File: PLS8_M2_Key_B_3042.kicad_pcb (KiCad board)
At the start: 10 copper layers, 42 x 30 mm, 39 parts, among them Q2 DTC123JUA, Q3 DTC123JUA, Q4 DTC123JUA, U20 PLS8-E, U28 M2_KEYB_3042

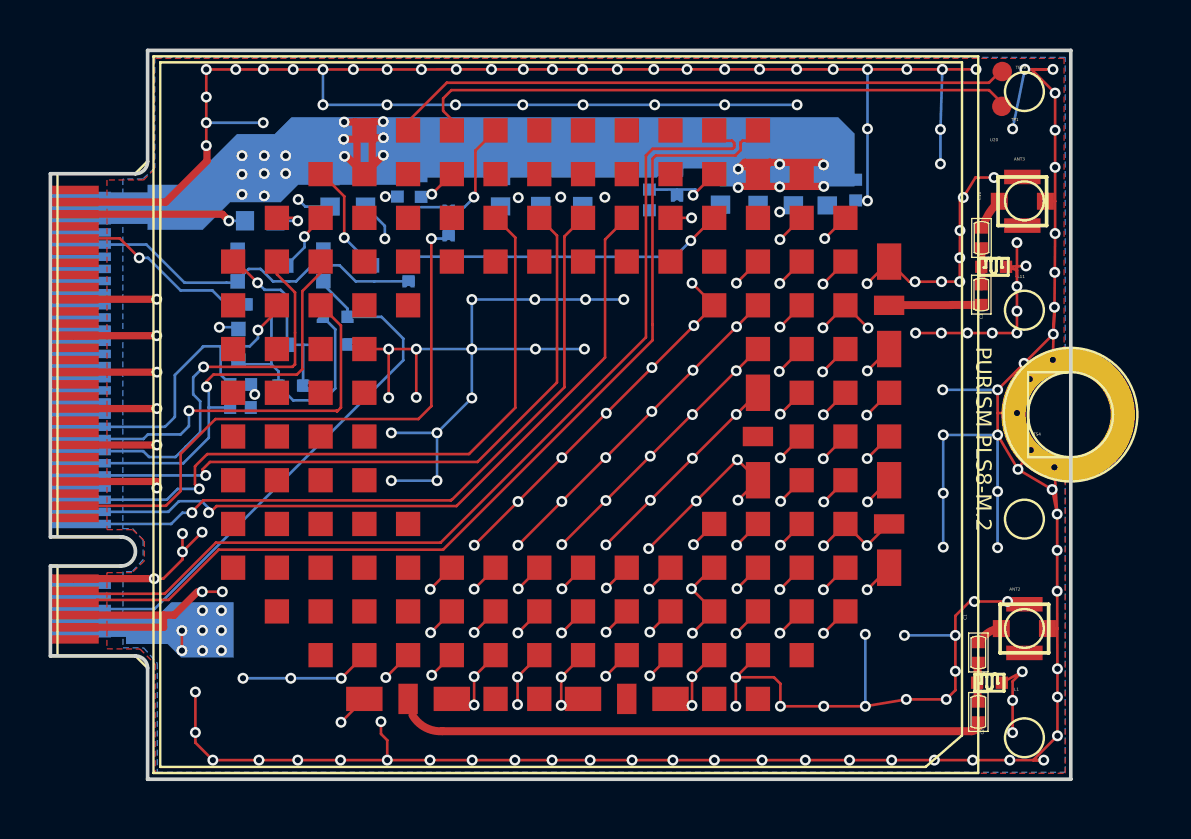
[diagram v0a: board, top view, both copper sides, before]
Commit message: Update the footprints in the layout using the ones assigned in the previous commit
Make C7 10nF as it was previously.
Fix the copper pour settings to make sure all connections are properly
made.
Adjust ATN2 and ANT3's footprint to have an underlying pad which copper
pour can connect to.
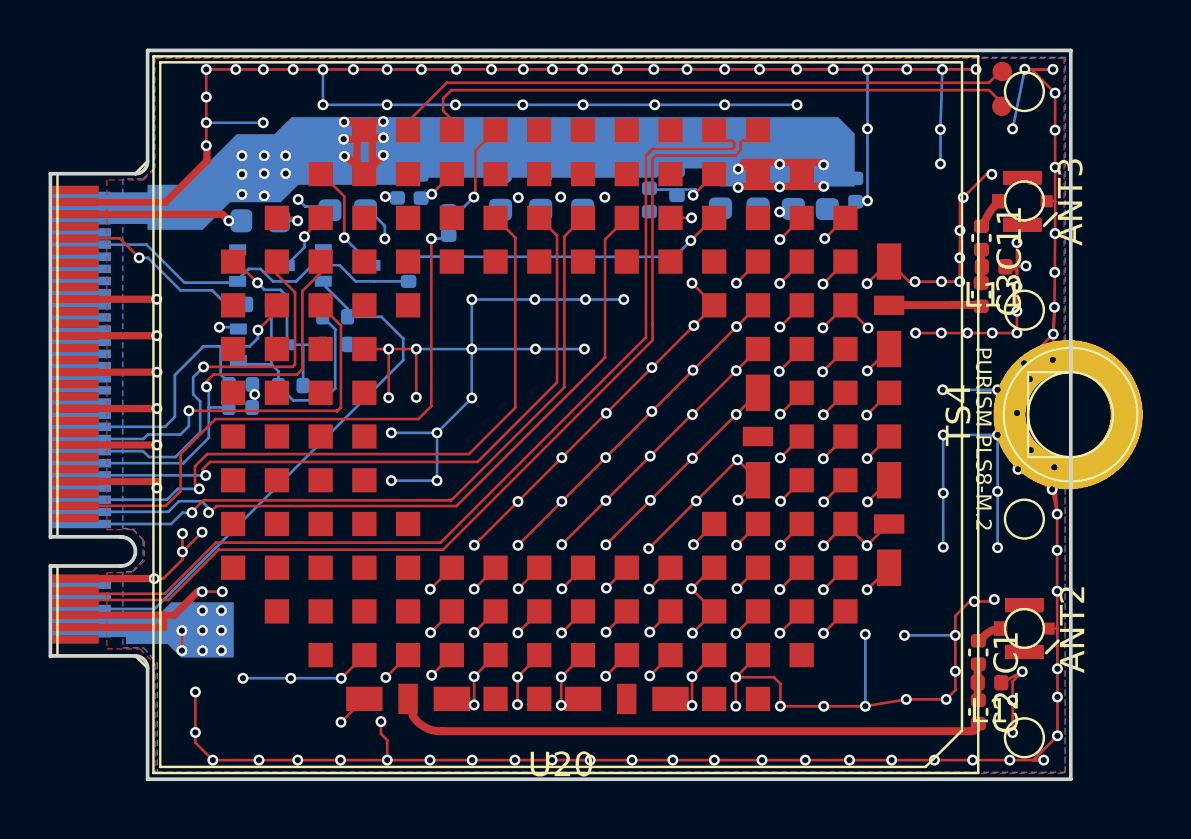
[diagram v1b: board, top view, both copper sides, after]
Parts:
- ANT2, ANT3: value APEX-4 -> MHF4; footprint APEX-4 -> PLS8_M2_Key_B_3042:MHF4_20449-001E
- C1, C11, C2, C3: value CAP-0402 -> 18pF; footprint CAP-0402 -> Capacitor_SMD:C_0402_1005Metric
- C10, C281, C283, C290, C299, C306, C329, C330, C4, C9: value CAP-0603 -> 22uF; footprint CAP-0603 -> Capacitor_SMD:C_0603_1608Metric
- C335, C5, C8: value CAP-0402 -> 220nF; footprint CAP-0402 -> Capacitor_SMD:C_0402_1005Metric
- C336, C6, C7: value CAP-0402 -> 10nF; footprint CAP-0402 -> Capacitor_SMD:C_0402_1005Metric
- L1, L11: value IND-0402 -> 22nH; footprint IND-0402 -> Inductor_SMD:L_0402_1005Metric
- Q2, Q4: value DTC123JUA -> DMN61D9UWQ-13; footprint DTC123JUA -> Package_TO_SOT_SMD:SOT-323_SC-70
- Q3: value DTC123JUA -> NC; footprint DTC123JUA -> Package_TO_SOT_SMD:SOT-323_SC-70
- R1, R133, R3, R4: value RES-0402 -> NC; footprint RES-0402 -> Resistor_SMD:R_0402_1005Metric
- R2, R5: value RES-0402 -> 100; footprint RES-0402 -> Resistor_SMD:R_0402_1005Metric
- R223: value RES-0402 -> 1k; footprint RES-0402 -> Resistor_SMD:R_0402_1005Metric
- TP1, TP39: value SIP-1PF -> TestPoint; footprint SIP-1PF -> PLS8_M2_Key_B_3042:TEST_POINT
- TS4: value SC-M4B -> MountingHole_Pad; footprint SC-M4B -> PLS8_M2_Key_B_3042:M.2_Mounting_Hole
- U20: value PLS8-E -> PLS8; footprint PLS8-E -> PLS8_M2_Key_B_3042:PLS8
- U28: value M2_KEYB_3042 -> M2_KEYB; footprint M2_KEYB_3042 -> PLS8_M2_Key_B_3042:M2_KEYB_3042
- moved Q2 1.19 mm to (147.3, 93.7), turned to 0 degrees
- moved Q3 1.19 mm to (150.9, 93.7), turned to 0 degrees
- moved Q4 1.19 mm to (147.4, 97.0), turned to 0 degrees
- turned ANT2 to -90 degrees
- turned ANT3 to -90 degrees
- turned C335 to 180 degrees
- turned L1 to 180 degrees
- turned L11 to 180 degrees
- turned R1 to 0 degrees
- turned R5 to 0 degrees
- turned TS4 to 90 degrees
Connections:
- net $$$1867 renamed Net-(R2-Pad2)
- net $$$21804 renamed Net-(C8-Pad1)
- net $$$27039 renamed Net-(TP39-Pad1)
- net $$$27041 renamed Net-(TP1-Pad1)
- net $$$30089 renamed Net-(C330-Pad1)
- net $$$30771 renamed Net-(Q2-Pad1)
- net $$$331 renamed Net-(Q3-Pad3)
- net $$$5364 renamed Net-(C3-Pad2)
- net $$$5383 renamed Net-(C2-Pad2)
- net 4G_ON/OFF renamed 4G_ON/OFF
- net CC1O renamed CCIO
- ANT2 pad 1: GND -> Net-(ANT2-Pad1)
- ANT2 pad 2: $$$5387 -> GND
- ANT3 pad 1: GND -> Net-(ANT3-Pad1)
- ANT3 pad 2: $$$5368 -> GND
- C1 pad 1: $$$5387 -> Net-(ANT2-Pad1)
- C1 pad 2: $$$5384 -> Net-(C1-Pad2)
- C11 pad 1: $$$5368 -> Net-(ANT3-Pad1)
- C11 pad 2: $$$5366 -> Net-(C11-Pad2)
- C2 pad 1: $$$5384 -> Net-(C1-Pad2)
- C3 pad 1: $$$5366 -> Net-(C11-Pad2)
- C335 pad 1: CCVCC -> GND
- C335 pad 2: GND -> CCVCC
- L1 pad 1: $$$5384 -> GND
- L1 pad 2: GND -> Net-(C1-Pad2)
- L11 pad 1: $$$5366 -> GND
- L11 pad 2: GND -> Net-(C11-Pad2)
- Q4 pad 1: $$$7885 -> Net-(Q4-Pad1)
- Q4 pad 3: $$$2935 -> Net-(Q4-Pad3)
- R1 pad 1: GND -> Net-(Q4-Pad3)
- R1 pad 2: $$$2935 -> GND
- R3 pad 2: $$$7885 -> Net-(Q4-Pad1)
- R4 pad 1: $$$7885 -> Net-(Q4-Pad1)
- R4 pad 2: $$$2935 -> Net-(Q4-Pad3)
- R5 pad 1: $$$7885 -> 4G_RESET
- R5 pad 2: 4G_RESET -> Net-(Q4-Pad1)
- U20 pad A4: (no net) -> unconnected-(U20-PadA4)
- U20 pad A7: (no net) -> unconnected-(U20-PadA7)
- U20 pad B14: (no net) -> unconnected-(U20-PadB14)
- U20 pad B3: (no net) -> unconnected-(U20-PadB3)
- U20 pad C12: (no net) -> unconnected-(U20-PadC12)
- U20 pad C13: (no net) -> unconnected-(U20-PadC13)
- U20 pad C14: (no net) -> unconnected-(U20-PadC14)
- U20 pad C15: (no net) -> unconnected-(U20-PadC15)
- U20 pad D12: (no net) -> unconnected-(U20-PadD12)
- U20 pad D13: (no net) -> unconnected-(U20-PadD13)
- U20 pad D14: (no net) -> unconnected-(U20-PadD14)
- U20 pad D15: (no net) -> unconnected-(U20-PadD15)
- U20 pad D16: (no net) -> unconnected-(U20-PadD16)
- U20 pad E12: (no net) -> unconnected-(U20-PadE12)
- U20 pad E13: (no net) -> unconnected-(U20-PadE13)
- U20 pad E14: (no net) -> unconnected-(U20-PadE14)
- U20 pad E15: (no net) -> unconnected-(U20-PadE15)
- U20 pad E16: (no net) -> unconnected-(U20-PadE16)
- U20 pad F13: (no net) -> unconnected-(U20-PadF13)
- U20 pad F14: (no net) -> unconnected-(U20-PadF14)
- U20 pad F15: (no net) -> unconnected-(U20-PadF15)
- U20 pad F16: (no net) -> unconnected-(U20-PadF16)
- U20 pad G13: (no net) -> unconnected-(U20-PadG13)
- U20 pad G14: (no net) -> unconnected-(U20-PadG14)
- U20 pad G15: (no net) -> unconnected-(U20-PadG15)
- U20 pad G16: (no net) -> unconnected-(U20-PadG16)
- U20 pad G4: (no net) -> unconnected-(U20-PadG4)
- U20 pad H13: (no net) -> unconnected-(U20-PadH13)
- U20 pad H14: (no net) -> unconnected-(U20-PadH14)
- U20 pad H15: (no net) -> unconnected-(U20-PadH15)
- U20 pad H16: (no net) -> unconnected-(U20-PadH16)
- U20 pad J14: (no net) -> unconnected-(U20-PadJ14)
- U20 pad J15: (no net) -> unconnected-(U20-PadJ15)
- U20 pad J16: (no net) -> unconnected-(U20-PadJ16)
- U20 pad K12: (no net) -> unconnected-(U20-PadK12)
- U20 pad K13: (no net) -> unconnected-(U20-PadK13)
- U20 pad K16: (no net) -> unconnected-(U20-PadK16)
- U20 pad L10: (no net) -> unconnected-(U20-PadL10)
- U20 pad L11: (no net) -> unconnected-(U20-PadL11)
- U20 pad L12: (no net) -> unconnected-(U20-PadL12)
- U20 pad L13: (no net) -> unconnected-(U20-PadL13)
- U20 pad L16: $$$2935 -> Net-(Q4-Pad3)
- U20 pad L5: (no net) -> unconnected-(U20-PadL5)
- U20 pad L6: (no net) -> unconnected-(U20-PadL6)
- U20 pad L7: (no net) -> unconnected-(U20-PadL7)
- U20 pad L8: (no net) -> unconnected-(U20-PadL8)
- U20 pad L9: (no net) -> unconnected-(U20-PadL9)
- U20 pad M11: (no net) -> unconnected-(U20-PadM11)
- U20 pad M12: (no net) -> unconnected-(U20-PadM12)
- U20 pad M13: (no net) -> unconnected-(U20-PadM13)
- U20 pad M4: (no net) -> unconnected-(U20-PadM4)
- U20 pad N10: (no net) -> unconnected-(U20-PadN10)
- U20 pad N12: (no net) -> unconnected-(U20-PadN12)
- U20 pad N6: (no net) -> unconnected-(U20-PadN6)
- U20 pad N7: (no net) -> unconnected-(U20-PadN7)
- U20 pad N8: (no net) -> unconnected-(U20-PadN8)
- U20 pad N9: (no net) -> unconnected-(U20-PadN9)
- U20 pad P6: (no net) -> unconnected-(U20-PadP6)
- U20 pad P7: (no net) -> unconnected-(U20-PadP7)
- U20 pad P8: (no net) -> unconnected-(U20-PadP8)
- U20 pad P9: (no net) -> unconnected-(U20-PadP9)
- U28 pad 1: (no net) -> unconnected-(U28-Pad1)
- U28 pad 10: (no net) -> unconnected-(U28-Pad10)
- U28 pad 21: (no net) -> unconnected-(U28-Pad21)
- U28 pad 25: (no net) -> unconnected-(U28-Pad25)
- U28 pad 26: (no net) -> unconnected-(U28-Pad26)
- U28 pad 29: (no net) -> unconnected-(U28-Pad29)
- U28 pad 31: (no net) -> unconnected-(U28-Pad31)
- U28 pad 35: (no net) -> unconnected-(U28-Pad35)
- U28 pad 37: (no net) -> unconnected-(U28-Pad37)
- U28 pad 38: (no net) -> unconnected-(U28-Pad38)
- U28 pad 40: (no net) -> unconnected-(U28-Pad40)
- U28 pad 41: (no net) -> unconnected-(U28-Pad41)
- U28 pad 42: (no net) -> unconnected-(U28-Pad42)
- U28 pad 43: (no net) -> unconnected-(U28-Pad43)
- U28 pad 44: (no net) -> unconnected-(U28-Pad44)
- U28 pad 46: (no net) -> unconnected-(U28-Pad46)
- U28 pad 47: (no net) -> unconnected-(U28-Pad47)
- U28 pad 48: (no net) -> unconnected-(U28-Pad48)
- U28 pad 49: (no net) -> unconnected-(U28-Pad49)
- U28 pad 50: (no net) -> unconnected-(U28-Pad50)
- U28 pad 52: (no net) -> unconnected-(U28-Pad52)
- U28 pad 53: (no net) -> unconnected-(U28-Pad53)
- U28 pad 54: (no net) -> unconnected-(U28-Pad54)
- U28 pad 55: (no net) -> unconnected-(U28-Pad55)
- U28 pad 56: (no net) -> unconnected-(U28-Pad56)
- U28 pad 58: (no net) -> unconnected-(U28-Pad58)
- U28 pad 59: (no net) -> unconnected-(U28-Pad59)
- U28 pad 60: (no net) -> unconnected-(U28-Pad60)
- U28 pad 61: (no net) -> unconnected-(U28-Pad61)
- U28 pad 62: (no net) -> unconnected-(U28-Pad62)
- U28 pad 63: (no net) -> unconnected-(U28-Pad63)
- U28 pad 64: (no net) -> unconnected-(U28-Pad64)
- U28 pad 65: (no net) -> unconnected-(U28-Pad65)
- U28 pad 68: (no net) -> unconnected-(U28-Pad68)
- U28 pad 69: (no net) -> unconnected-(U28-Pad69)
- U28 pad 75: (no net) -> unconnected-(U28-Pad75)
- U28 pad 8: (no net) -> unconnected-(U28-Pad8)
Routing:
- net $$$7885: track 11.0 -> 0.00 mm
- net Net-(Q4-Pad1): track 0.00 -> 11.0 mm
- net $$$2935: track 7.98 -> 0.00 mm, vias 1 -> 0
- net Net-(Q4-Pad3): track 0.00 -> 7.96 mm, vias 0 -> 1
- net VBAT: track 111.4 -> 117.8 mm
- net Net-(C11-Pad2): track 0.00 -> 1.87 mm
- net $$$5366: track 1.87 -> 0.00 mm
- net Net-(C1-Pad2): track 0.00 -> 1.49 mm
- net $$$5384: track 1.49 -> 0.00 mm
- net Net-(ANT3-Pad1): track 0.00 -> 1.36 mm
- net $$$5368: track 1.36 -> 0.00 mm
- net Net-(ANT2-Pad1): track 0.00 -> 1.15 mm
- net $$$5387: track 1.15 -> 0.00 mm
- net Net-(R2-Pad2): track 5.48 -> 4.41 mm
- net GND: track 439.7 -> 439.1 mm

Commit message: Fix all of the DRC violations.
Made exceptions for courtyard overlaps where the components have not
moved. Some components have been moved slightly to accomidate a minimum
5mil soldermask sliver (especially due to the slightly larger pad sizes
given in KiCad's footprint library).

All silkscreen related-warnings have been ignored. The silkscreen
reference designator text still needs to be moved.
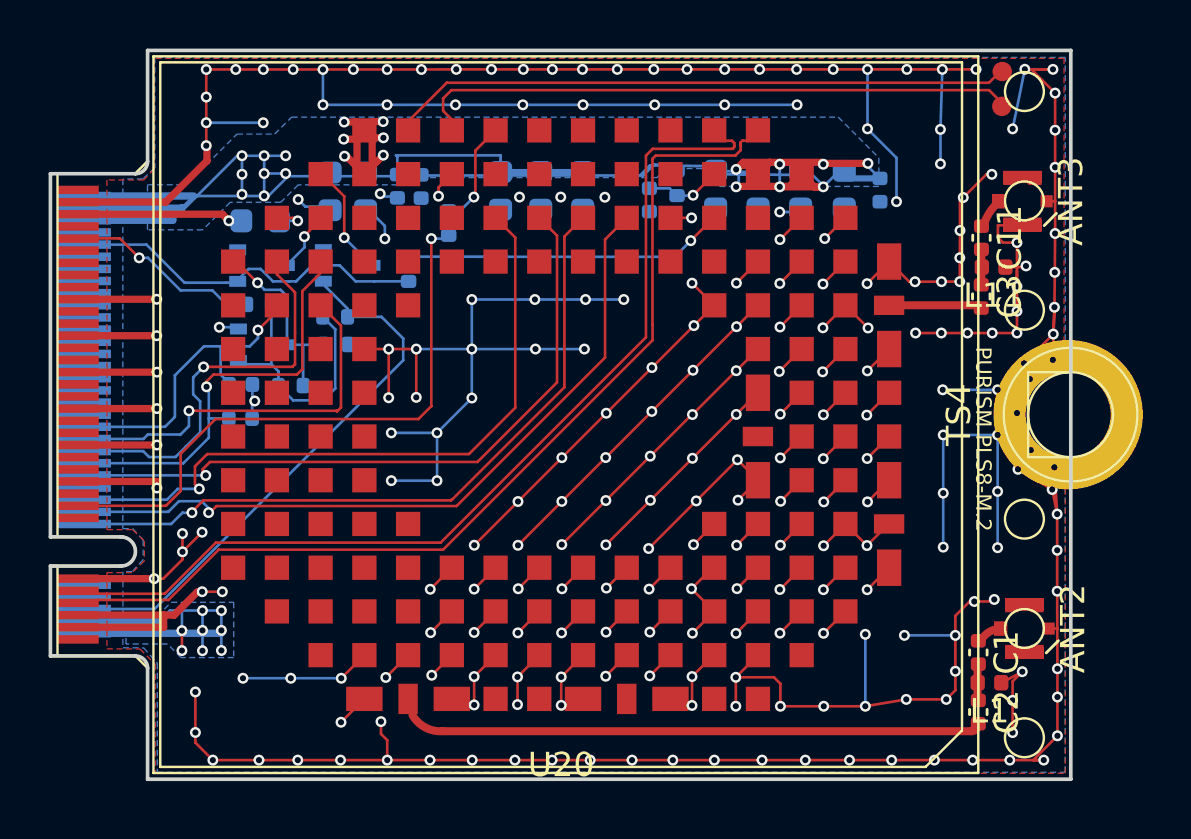
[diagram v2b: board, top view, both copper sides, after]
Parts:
- moved C7 1.00 mm to (172.8, 90.6)
- moved C299 0.70 mm to (171.3, 90.6)
- moved C336 0.45 mm to (146.5, 100.0)
- moved C306 0.30 mm to (169.5, 90.6)
- moved C281 0.20 mm to (166.0, 90.6)
- moved C3 0.08 mm to (177.0, 95.0)
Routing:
- net VBAT: track 117.8 -> 123.1 mm, vias 28 -> 29
- net GND: track 439.1 -> 442.7 mm
- added copper zone on In2.Cu, net GND
- added copper zone on B.Cu, net VBAT
- added copper zone on In2.Cu, net VBAT
- removed copper zone on In8.Cu, net GND
- removed copper zone on In8.Cu, net VBAT
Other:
- copper layers 10 -> 4

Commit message: Fix up the silkscreen and use a board stackup that has a thickness of 0.8mm
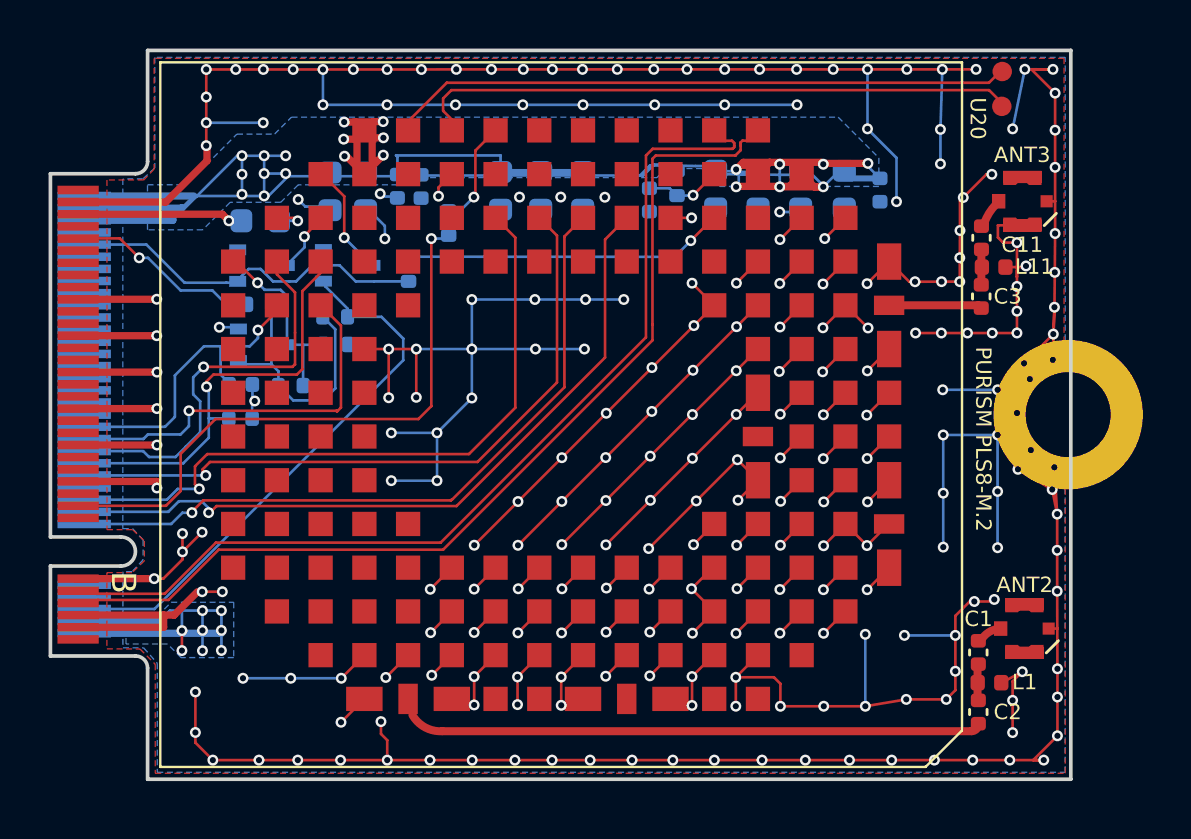
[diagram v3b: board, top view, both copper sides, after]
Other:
- board text added: "B"
